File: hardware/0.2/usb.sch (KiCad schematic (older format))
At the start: 34 parts, among them J2 USB_C_Receptacle_USB2.0, J3 USB_C_Receptacle_USB2.0, J4 USB_C_Receptacle_USB2.0, U5 CY7C65632-28LTXCT, U6 USBLC6-2SC6, U7 USBLC6-2SC6, U8 USBLC6-2SC6, Y2 12MHz

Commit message: layout getting close
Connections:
- net +3V3 renamed +3.3VP
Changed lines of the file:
@@
 $EndComp
 $Comp
-L power:+3V3 #PWR0127
-U 1 1 5F665451
+L power:+3.3VP #PWR0127
+U 1 1 5F6AC15C
 P 3600 1600
-F 0 "#PWR0127" H 3600 1450 50  0001 C CNN
-F 1 "+3V3" H 3615 1773 50  0000 C CNN
+F 0 "#PWR0127" H 3750 1550 50  0001 C CNN
+F 1 "+3.3VP" H 3615 1773 50  0000 C CNN
 F 2 "" H 3600 1600 50  0001 C CNN
 F 3 "" H 3600 1600 50  0001 C CNN
@@
 $EndComp
 $Comp
-L power:+3V3 #PWR0131
-U 1 1 5F66FC10
+L power:+3.3VP #PWR0131
+U 1 1 5F6ACBA4
+P 1350 6625
+F 0 "#PWR0131" H 1500 6575 50  0001 C CNN
+F 1 "+3.3VP" H 1365 6798 50  0000 C CNN
+F 2 "" H 1350 6625 50  0001 C CNN
+F 3 "" H 1350 6625 50  0001 C CNN
+	1    1350 6625
+	1    0    0    -1
+$EndComp
+$Comp
+L power:+3.3VP #PWR0133
+U 1 1 5F6AF66C
 P 4375 6625
-F 0 "#PWR0131" H 4375 6475 50  0001 C CNN
-F 1 "+3V3" H 4390 6798 50  0000 C CNN
+F 0 "#PWR0133" H 4525 6575 50  0001 C CNN
+F 1 "+3.3VP" H 4390 6798 50  0000 C CNN
 F 2 "" H 4375 6625 50  0001 C CNN
 F 3 "" H 4375 6625 50  0001 C CNN
@@
 $EndComp
 $Comp
-L power:+3V3 #PWR0133
-U 1 1 5F68EA5F
-P 1350 6625
-F 0 "#PWR0133" H 1350 6475 50  0001 C CNN
-F 1 "+3V3" H 1365 6798 50  0000 C CNN
-F 2 "" H 1350 6625 50  0001 C CNN
-F 3 "" H 1350 6625 50  0001 C CNN
-	1    1350 6625
+L power:+3.3VP #PWR0147
+U 1 1 5F6B21F7
+P 6450 6750
+F 0 "#PWR0147" H 6600 6700 50  0001 C CNN
+F 1 "+3.3VP" H 6465 6923 50  0000 C CNN
+F 2 "" H 6450 6750 50  0001 C CNN
+F 3 "" H 6450 6750 50  0001 C CNN
+	1    6450 6750
 	1    0    0    -1
 $EndComp
 $Comp
-L power:+3V3 #PWR0136
-U 1 1 5F6B2C62
+L power:+3.3VP #PWR?
+U 1 1 5F6D74F0
 P 3550 2575
-F 0 "#PWR0136" H 3550 2425 50  0001 C CNN
-F 1 "+3V3" H 3565 2748 50  0000 C CNN
+F 0 "#PWR?" H 3700 2525 50  0001 C CNN
+F 1 "+3.3VP" H 3565 2748 50  0000 C CNN
 F 2 "" H 3550 2575 50  0001 C CNN
 F 3 "" H 3550 2575 50  0001 C CNN
@@
 	1    0    0    -1
 $EndComp
-$Comp
-L power:+3V3 #PWR0147
-U 1 1 5F6BCBEE
-P 6450 6750
-F 0 "#PWR0147" H 6450 6600 50  0001 C CNN
-F 1 "+3V3" H 6465 6923 50  0000 C CNN
-F 2 "" H 6450 6750 50  0001 C CNN
-F 3 "" H 6450 6750 50  0001 C CNN
-	1    6450 6750
-	1    0    0    -1
-$EndComp

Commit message: update BOM
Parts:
- C17, C18: value 22p -> 15p; DigiKey 1276-2228-1-ND -> 1276-1296-2-ND; LCSC C1653 -> C1644; MPN CL10C220JB8NFNC -> CL10C150JB8NNNC; Substitue Allowed? Y -> Y - NP0 / C0G
- C41: DigiKey 1276-1000-1-ND -> 1276-1871-1-ND; LCSC C1591 -> C85713; MPN CL10B104KB8NNNC -> CL10A106MP8NNNC; Substitue Allowed? Y -> Y - X5R or better
- C42: DigiKey 1276-1871-1-ND -> 1276-1000-1-ND; LCSC C85713 -> C1591; MPN CL10A106MP8NNNC -> CL10B104KB8NNNC; Substitue Allowed? Y -> Y - X5R or better
- C43, C46, C47, C54, C55, C56, C57: Substitue Allowed? Y -> Y - X5R or better
- C58, C59, C60: DigiKey (none) -> 1276-1000-1-ND; LCSC (none) -> C1591; MPN (none) -> CL10B104KB8NNNC; Manufacturer (none) -> Samsung Electro-Mechanics; Substitue Allowed? (none) -> Y - X5R or better
- F2, F3, F4: DigiKey (none) -> 507-1811-1-ND; LCSC (none) -> C70057; MPN (none) -> 0ZCK0020FF2G; Manufacturer (none) -> Bel Fuse; Notes (none) -> LCSC: Substitute PN; Substitue Allowed? (none) -> Y - 200mA hold / 500mA trip
- FB1, FB2, FB3, FB4: DigiKey 490-1014-1-ND -> 490-5258-1-ND; LCSC C19330 -> C85833; MPN BLM18AG601SN1D -> BLM18KG601SN1D; Substitue Allowed? Y -> Y - 600R, > 1A current
- J2, J3, J4: Substitue Allowed? Y -> Y - Footprint / pinout compatiable
- R10, RN3: Substitue Allowed? Y -> Y - Same spec
- R7: DigiKey CR0603-JW-104ELFCT-ND -> CR0603-JW-103ELFCT-ND; LCSC C203223 -> C144116; MPN CR0603-JW-104ELF -> CR0603-JW-103ELF; Substitue Allowed? Y -> Y - Same spec
- R8, R9: DigiKey (none) -> CR0603-JW-103ELFCT-ND; LCSC (none) -> C144116; MPN (none) -> CR0603-JW-103ELF; Manufacturer (none) -> Bourns; Notes (none) -> LCSC: Substitute PN; Substitue Allowed? (none) -> Y - Same spec
- U6, U7, U8: Manufacturer STmicroelectronics -> STMicroelectronics; Substitue Allowed? (none) -> N
- Y2: DigiKey 535-9826-1-ND -> 535-14962-6-ND; LCSC C276421 -> C164041; MPN ABM8-12.000MHZ-B2-T -> ABM8-12.000MHZ-12-B1U-T; Notes (none) -> LCSC: Substitute PN; Substitue Allowed? Y -> Y - 12 MHz, 10/12pF

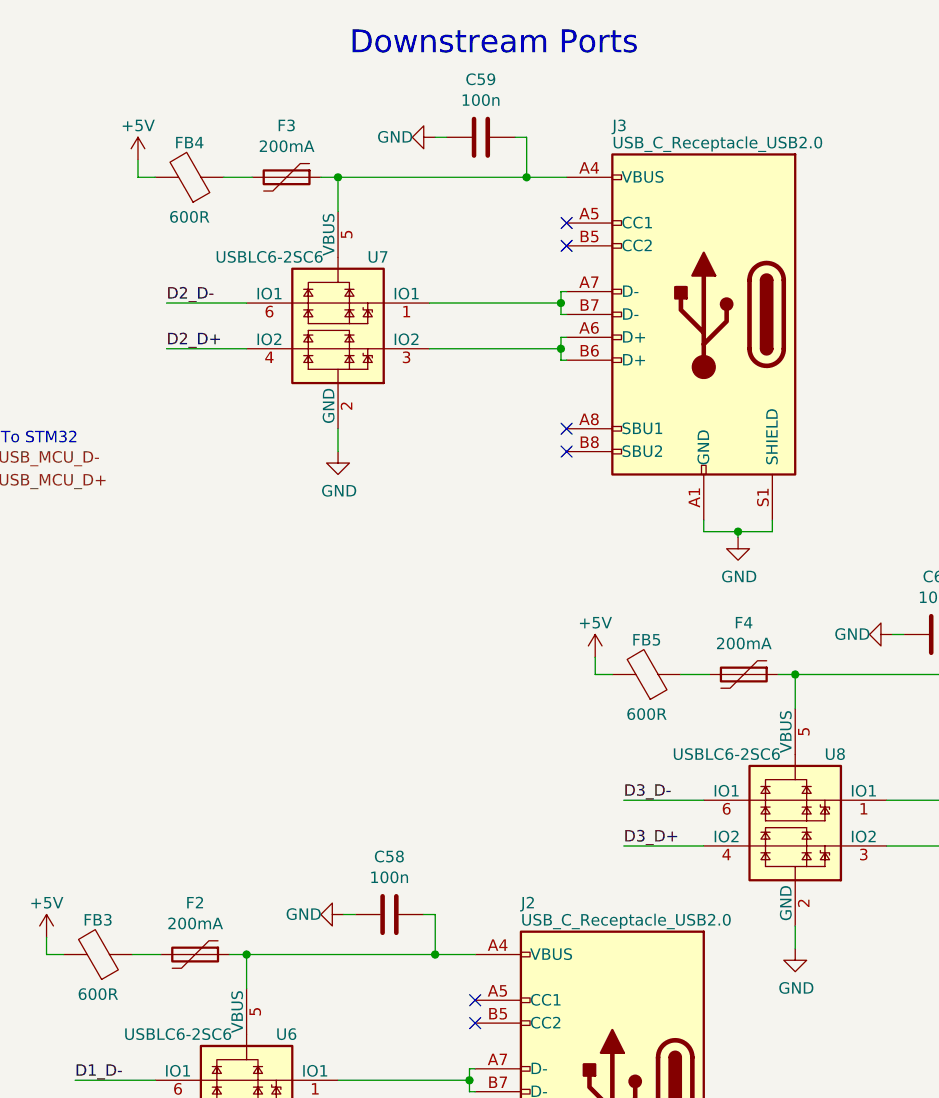
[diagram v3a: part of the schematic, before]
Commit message: update fuse values
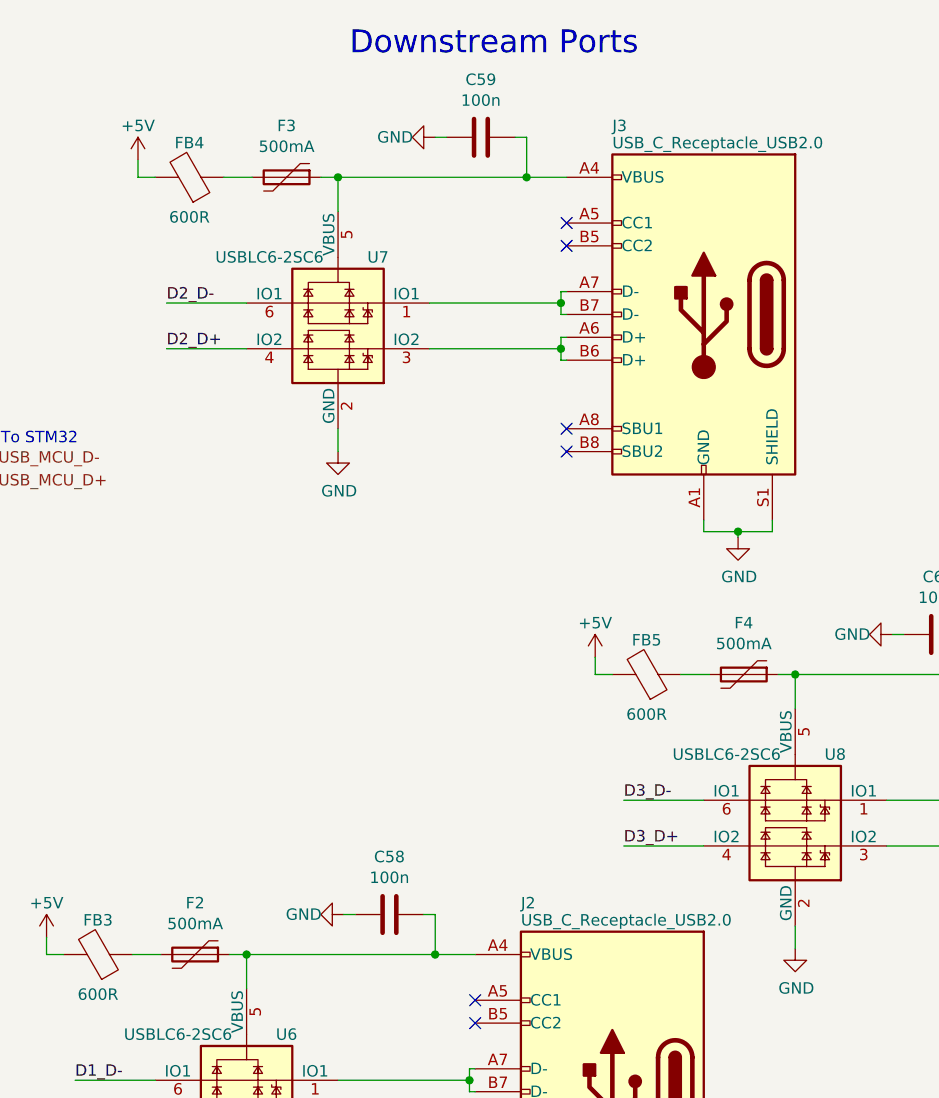
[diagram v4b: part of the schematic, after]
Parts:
- F2, F3, F4: value 200mA -> 500mA; DigiKey 507-1811-1-ND -> F2772CT-ND; LCSC C70057 -> C207022; MPN 0ZCK0020FF2G -> 0805L050WR; Manufacturer Bel Fuse -> Littelfuse; Notes LCSC: Substitute PN -> (none)
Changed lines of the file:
@@
 P 6700 1200
 F 0 "F3" V 6475 1200 50  0000 C CNN
-F 1 "200mA" V 6566 1200 50  0000 C CNN
+F 1 "500mA" V 6566 1200 50  0000 C CNN
 F 2 "josh-passives-smt:Fuse_0805_2012Metric" H 6750 1000 50  0001 L CNN
 F 3 "~" H 6700 1200 50  0001 C CNN
-F 4 "507-1811-1-ND" H 6700 1200 50  0001 C CNN "DigiKey"
-F 5 "C70057" H 6700 1200 50  0001 C CNN "LCSC"
-F 6 "0ZCK0020FF2G" H 6700 1200 50  0001 C CNN "MPN"
-F 7 "Bel Fuse" H 6700 1200 50  0001 C CNN "Manufacturer"
-F 8 "LCSC: Substitute PN" H 6700 1200 50  0001 C CNN "Notes"
+F 4 "F2772CT-ND" H 6700 1200 50  0001 C CNN "DigiKey"
+F 5 "C207022" H 6700 1200 50  0001 C CNN "LCSC"
+F 6 "0805L050WR" H 6700 1200 50  0001 C CNN "MPN"
+F 7 "Littelfuse" H 6700 1200 50  0001 C CNN "Manufacturer"
+F 8 "" H 6700 1200 50  0001 C CNN "Notes"
 F 9 "Y - 200mA hold / 500mA trip" H 6700 1200 50  0001 C CNN "Substitue Allowed?"
 	1    6700 1200
@@
 P 8700 3375
 F 0 "F4" V 8475 3375 50  0000 C CNN
-F 1 "200mA" V 8566 3375 50  0000 C CNN
+F 1 "500mA" V 8566 3375 50  0000 C CNN
 F 2 "josh-passives-smt:Fuse_0805_2012Metric" H 8750 3175 50  0001 L CNN
 F 3 "~" H 8700 3375 50  0001 C CNN
-F 4 "507-1811-1-ND" H 8700 3375 50  0001 C CNN "DigiKey"
-F 5 "C70057" H 8700 3375 50  0001 C CNN "LCSC"
-F 6 "0ZCK0020FF2G" H 8700 3375 50  0001 C CNN "MPN"
-F 7 "Bel Fuse" H 8700 3375 50  0001 C CNN "Manufacturer"
-F 8 "LCSC: Substitute PN" H 8700 3375 50  0001 C CNN "Notes"
+F 4 "F2772CT-ND" H 8700 3375 50  0001 C CNN "DigiKey"
+F 5 "C207022" H 8700 3375 50  0001 C CNN "LCSC"
+F 6 "0805L050WR" H 8700 3375 50  0001 C CNN "MPN"
+F 7 "Littelfuse" H 8700 3375 50  0001 C CNN "Manufacturer"
+F 8 "" H 8700 3375 50  0001 C CNN "Notes"
 F 9 "Y - 200mA hold / 500mA trip" H 8700 3375 50  0001 C CNN "Substitue Allowed?"
 	1    8700 3375
@@
 P 6300 4600
 F 0 "F2" V 6075 4600 50  0000 C CNN
-F 1 "200mA" V 6166 4600 50  0000 C CNN
+F 1 "500mA" V 6166 4600 50  0000 C CNN
 F 2 "josh-passives-smt:Fuse_0805_2012Metric" H 6350 4400 50  0001 L CNN
 F 3 "~" H 6300 4600 50  0001 C CNN
-F 4 "507-1811-1-ND" H 6300 4600 50  0001 C CNN "DigiKey"
-F 5 "C70057" H 6300 4600 50  0001 C CNN "LCSC"
-F 6 "0ZCK0020FF2G" H 6300 4600 50  0001 C CNN "MPN"
-F 7 "Bel Fuse" H 6300 4600 50  0001 C CNN "Manufacturer"
-F 8 "LCSC: Substitute PN" H 6300 4600 50  0001 C CNN "Notes"
+F 4 "F2772CT-ND" H 6300 4600 50  0001 C CNN "DigiKey"
+F 5 "C207022" H 6300 4600 50  0001 C CNN "LCSC"
+F 6 "0805L050WR" H 6300 4600 50  0001 C CNN "MPN"
+F 7 "Littelfuse" H 6300 4600 50  0001 C CNN "Manufacturer"
+F 8 "" H 6300 4600 50  0001 C CNN "Notes"
 F 9 "Y - 200mA hold / 500mA trip" H 6300 4600 50  0001 C CNN "Substitue Allowed?"
 	1    6300 4600
